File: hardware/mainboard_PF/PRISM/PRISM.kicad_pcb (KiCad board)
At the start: 2 copper layers, 47.4 x 47.4 mm, 1 part, among them U1 XC7Z010-3CLG400E

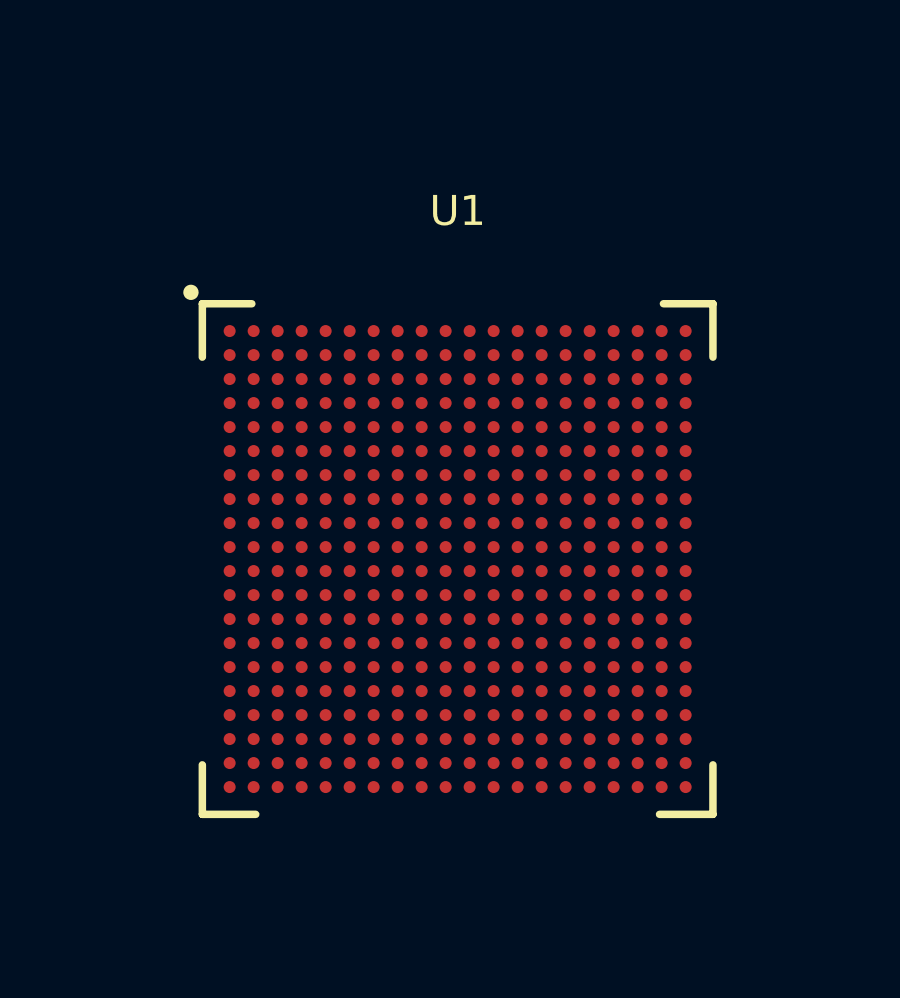
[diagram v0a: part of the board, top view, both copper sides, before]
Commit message: More Protoflow
Power Systesm
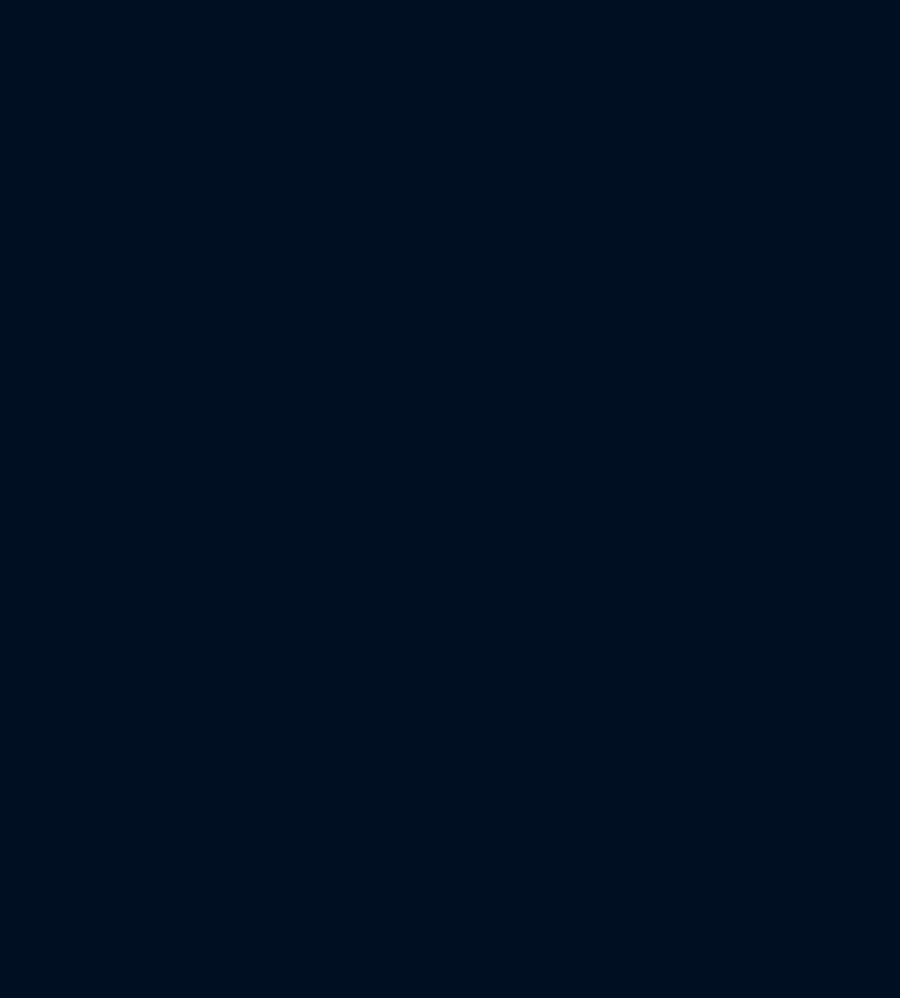
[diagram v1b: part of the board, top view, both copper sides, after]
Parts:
- removed U1: XC7Z010-3CLG400E, fasteda:FBGA-400_L17.0-W17.0-R20-C20-P0.80-TL
